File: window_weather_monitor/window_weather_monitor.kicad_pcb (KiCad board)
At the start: 2 copper layers, 180 x 120 mm, 66 parts, among them J1 Barrel_Jack, SW1 RST Switch, SW2 PWR DISABLE, U1 Adafruit_Feather_HUZZAH32_ESP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, U2 DHT11, U3 Rain Sensor, U6 LT1086-5.0

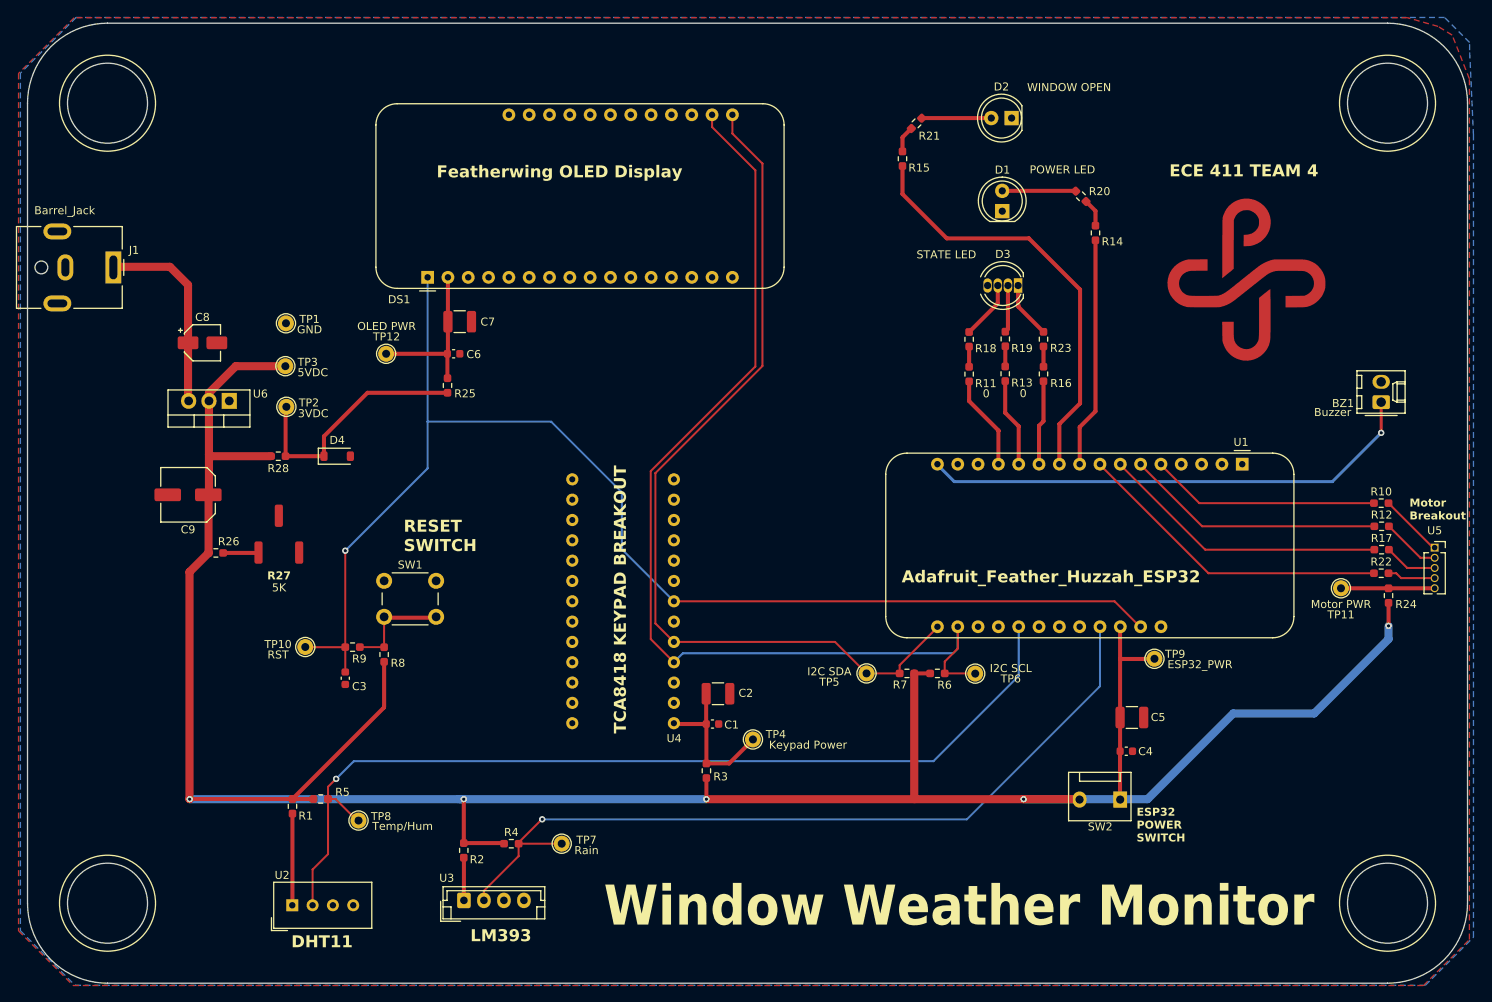
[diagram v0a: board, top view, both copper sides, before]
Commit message: Updated PCB
Updated the schematic, layout, generated gerber files for fab, added requisite info on PCB.
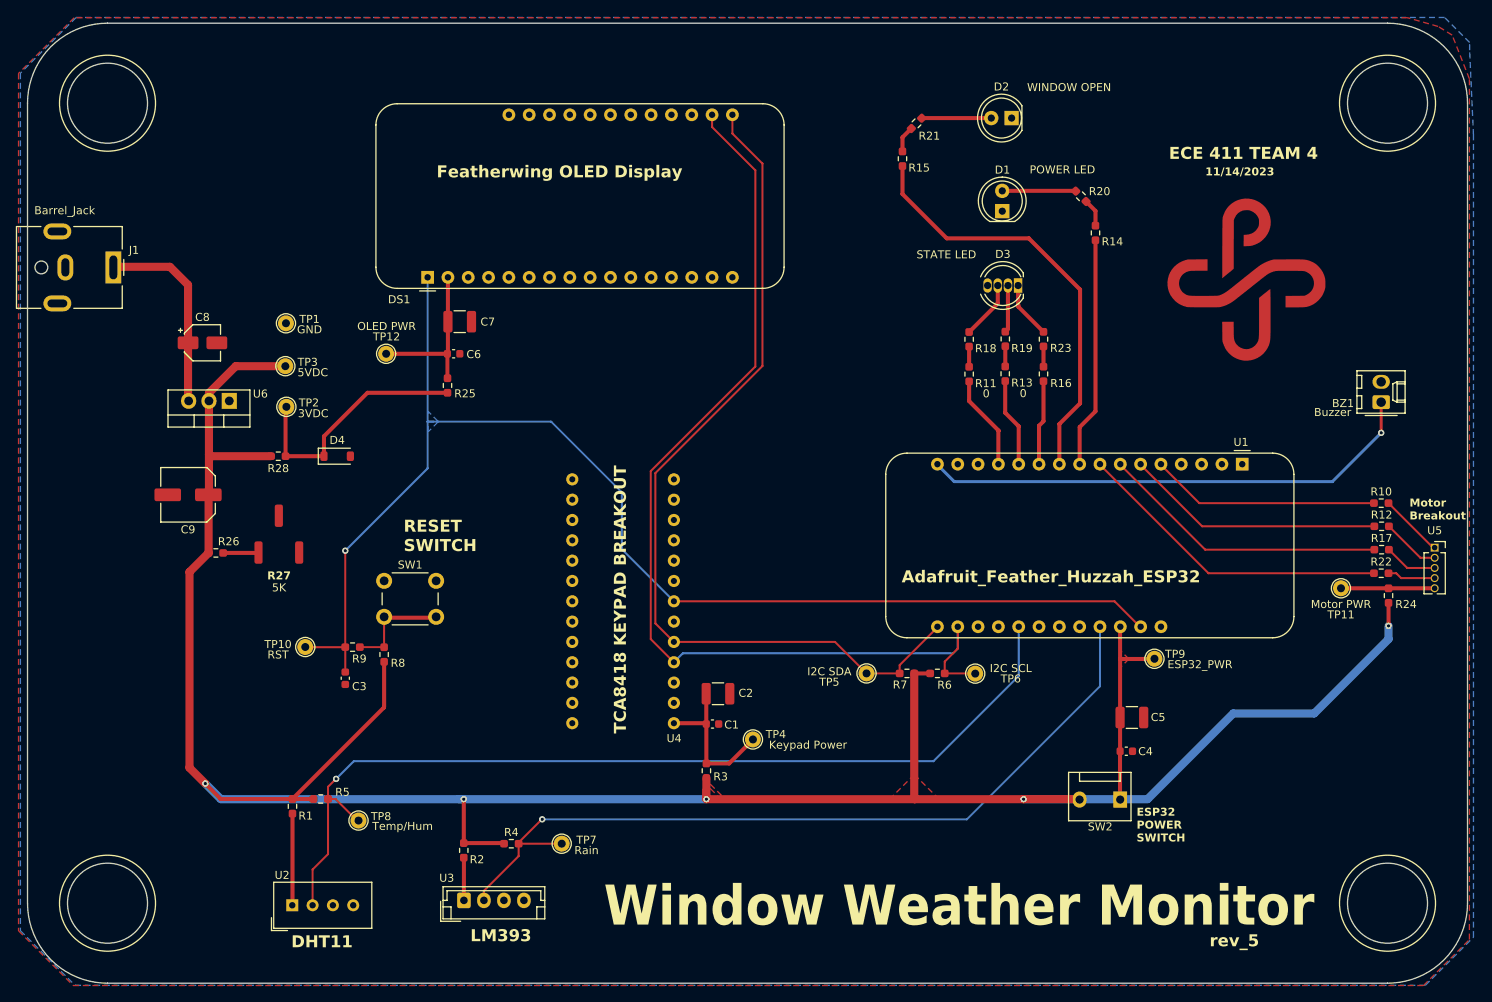
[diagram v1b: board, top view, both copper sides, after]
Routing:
- net /+5VDC: track 310.0 -> 306.5 mm
- added copper zone on F.Cu, net (none)
- added copper zone on F.Cu, net /+5VDC
- added copper zone on B.Cu, net RST SW
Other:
- board text added: "11/14/2023"
- board text added: "Team Members: Joshua Dworning Casey McGuire Mosiah Beal Joel Utecht Andy Nguyen"
- board text added: "rev_5"

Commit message: Changes to make a working board
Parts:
- D3: value STATE LED -> LED_RGBK
- U2: value DHT11 -> DHT22
- moved C8 4.07 mm to (52.3, 65.9)
- moved TP4 3.92 mm to (124.6, 119.5)
- moved R4 3.06 mm to (90.5, 129.5)
- moved R2 2.96 mm to (84.6, 130.4)
- moved C1 1.49 mm to (117.1, 117.6)
- moved C2 1.49 mm to (117.8, 113.8)
- moved C6 1.08 mm to (83.2, 72.4)
- moved C7 1.08 mm to (84.0, 68.4)
- moved R25 1.08 mm to (82.4, 76.4)
- moved D3 0.95 mm to (154.5, 62.1)
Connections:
- D3 pad 3: Net-(D3-BA) -> GND
- D3 pad 4: GND -> Net-(D3-BA)
- R14 pad 1: Net-(U1-IO36/A4) -> Net-(U1-A9/IO33)
- R17 pad 1: Net-(U1-I34/A2) -> Net-(U1-A6/IO14)
- R22 pad 1: Net-(U1-I39/A3) -> Net-(U1-A7/IO32)
- U1 pad 19: unconnected-(U1-A6/IO14-Pad19) -> Net-(U1-A6/IO14)
- U1 pad 20: unconnected-(U1-A7/IO32-Pad20) -> Net-(U1-A7/IO32)
- U1 pad 22: unconnected-(U1-A9/IO33-Pad22) -> Net-(U1-A9/IO33)
- U1 pad 7: Net-(U1-I34/A2) -> unconnected-(U1-I34/A2-Pad7)
- U1 pad 8: Net-(U1-I39/A3) -> unconnected-(U1-I39/A3-Pad8)
- U1 pad 9: Net-(U1-IO36/A4) -> unconnected-(U1-IO36/A4-Pad9)
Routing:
- net Net-(U1-A9/IO33): track 0.00 -> 92.9 mm, vias 0 -> 1
- net Net-(U1-A6/IO14): track 0.00 -> 55.3 mm, vias 0 -> 1
- net Net-(U1-A7/IO32): track 0.00 -> 51.4 mm, vias 0 -> 1
- net Net-(U1-I39/A3): track 39.9 -> 0.00 mm
- net Net-(U1-I34/A2): track 36.1 -> 0.00 mm
- net Net-(U1-IO36/A4): track 28.9 -> 0.00 mm
- net Net-(SW2-A): track 0.00 -> 28.2 mm, vias 0 -> 1
- net (no net): track 25.7 -> 0.00 mm
- net /+5VDC: track 306.5 -> 290.6 mm, vias 5 -> 2
- net Net-(U4-VIN): track 20.0 -> 26.7 mm, vias 0 -> 1
- net I2C SCL: track 126.4 -> 132.6 mm, vias 0 -> 3
- net Net-(R8-Pad2): track 12.5 -> 18.1 mm, vias 0 -> 1
- net I2C SDA: track 111.5 -> 116.5 mm, vias 0 -> 4
- net Net-(U3-VCC): track 5.35 -> 8.64 mm, vias 0 -> 1
- net Net-(U1-DAC1/A1): track 32.4 -> 34.2 mm, vias 0 -> 1
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- removed copper zone on F.Cu, net (none)
- removed copper zone on F.Cu, net /+5VDC
- removed copper zone on B.Cu, net RST SW
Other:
- outline, holes or cut-outs redrawn
- board text added: "rev_666"
- board text removed: "rev_5"
